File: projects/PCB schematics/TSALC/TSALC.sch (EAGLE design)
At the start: 27 parts, among them IC2 78L08SMD, IC4 NE555D, Q1 IRLZ44Z, Q2 IRLZ44Z, Q3 IRLZ44Z

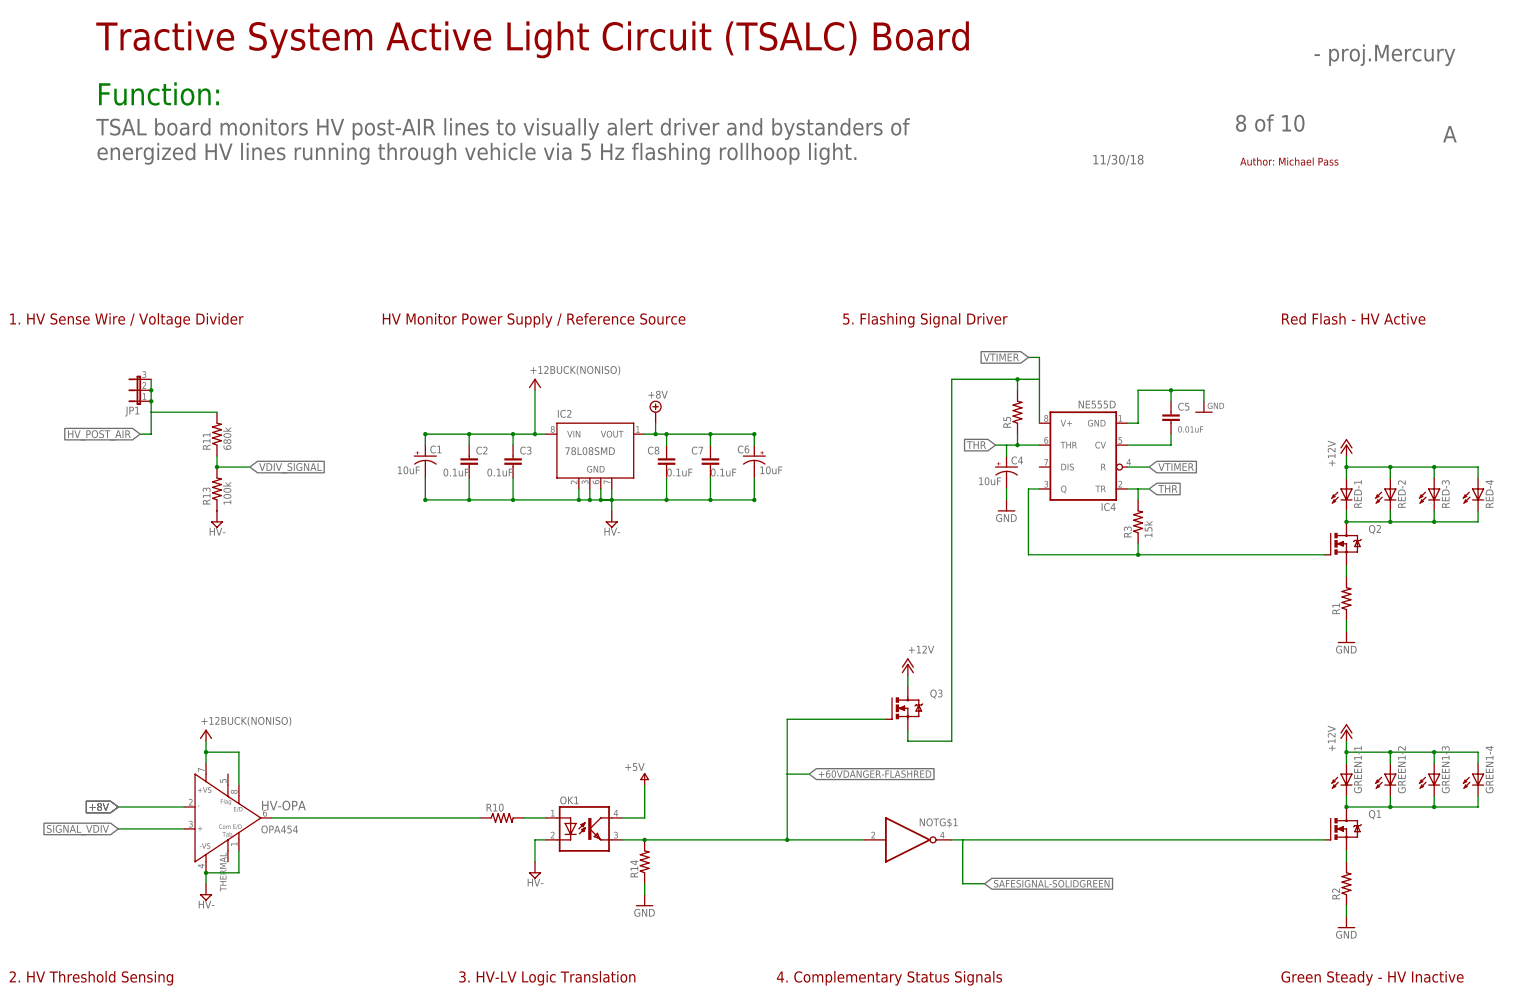
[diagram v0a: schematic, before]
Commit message: SC - Rev A; First PCB revision complete.
This marks the first draft of the SC board.
Parts have been laid out and initial routing completed through
extensive use of autorouter.
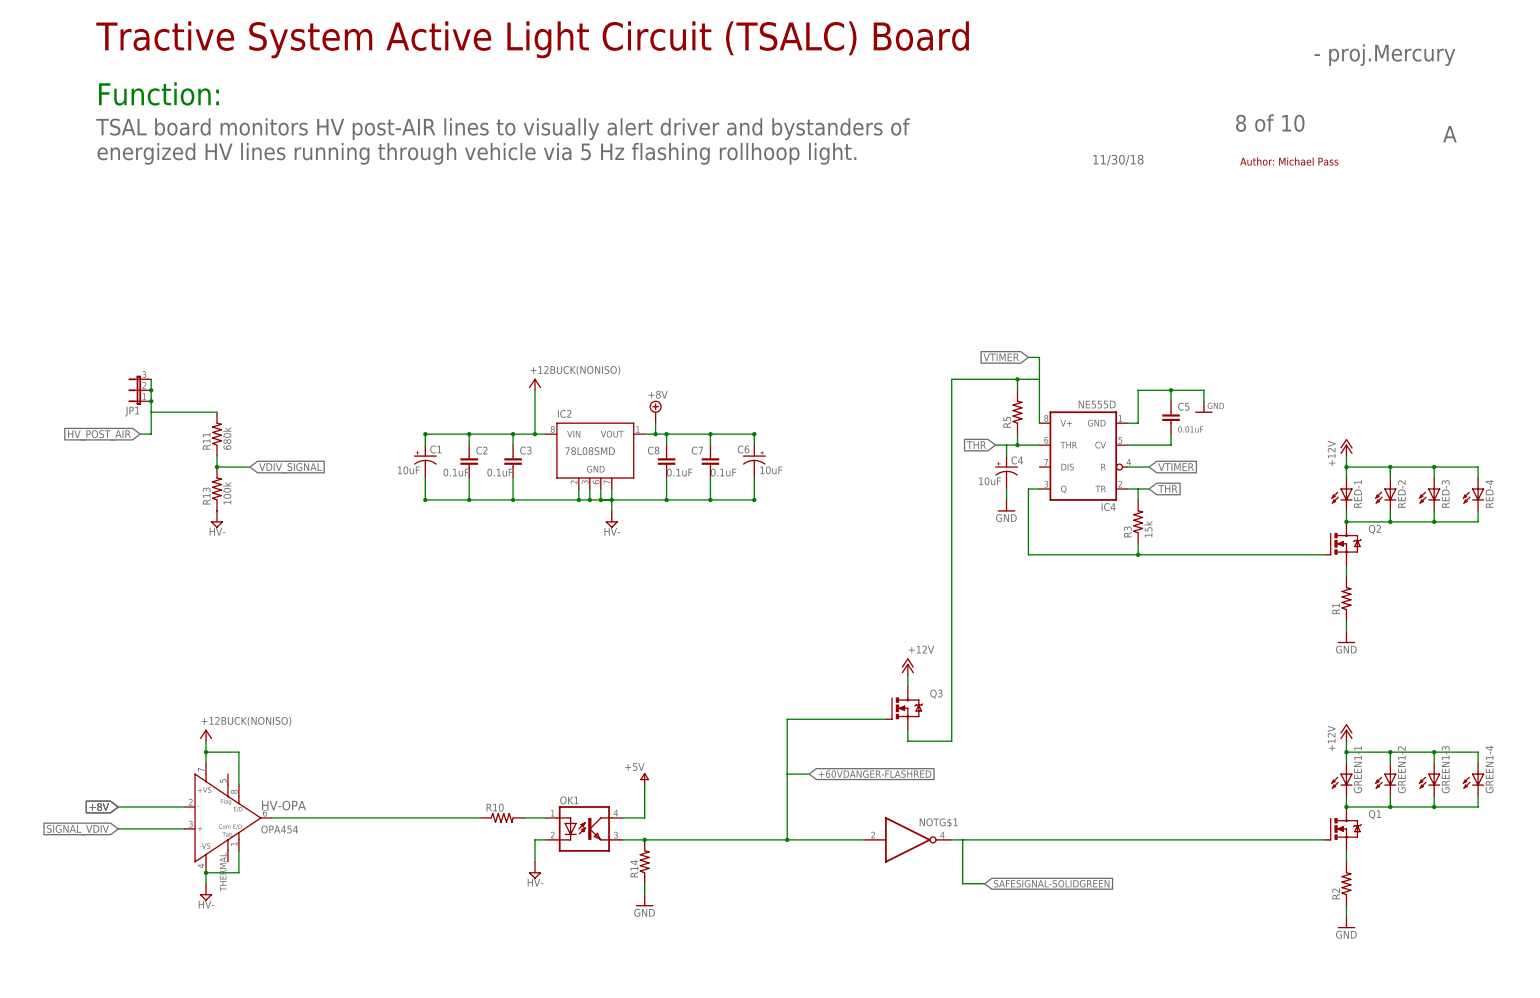
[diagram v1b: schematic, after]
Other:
- note removed: "1. HV Sense Wire / Voltage Divider"
- note removed: "2. HV Threshold Sensing"
- note removed: "3. HV-LV Logic Translation"
- note removed: "4. Complementary Status Signals"
- note removed: "5. Flashing Signal Driver"
- note removed: "Green Steady - HV Inactive"
- note removed: "HV Monitor Power Supply / Reference Source"
- note removed: "Red Flash - HV Active"
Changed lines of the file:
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@@
 <?xml version="1.0" encoding="utf-8"?>
 <!DOCTYPE eagle SYSTEM "eagle.dtd">
-<eagle version="9.3.0">
+<eagle version="9.3.1">
 <drawing>
 <settings>
@@
 <sheet>
 <plain>
-<frame x1="7.62" y1="7.62" x2="109.22" y2="81.28" columns="8" rows="5" layer="94" border-left="no" border-top="no" border-right="no" border-bottom="no"/>
-<text x="10.16" y="10.16" size="2.54" layer="94">2. HV Threshold Sensing</text>
-<frame x1="7.62" y1="7.62" x2="71.12" y2="15.24" columns="8" rows="5" layer="94" border-left="no" border-top="no" border-right="no" border-bottom="no"/>
-<frame x1="111.76" y1="7.62" x2="177.8" y2="81.28" columns="8" rows="5" layer="94" border-left="no" border-top="no" border-right="no" border-bottom="no"/>
-<text x="114.3" y="10.16" size="2.54" layer="94">3. HV-LV Logic Translation</text>
-<frame x1="111.76" y1="7.62" x2="177.8" y2="15.24" columns="8" rows="5" layer="94" border-left="no" border-top="no" border-right="no" border-bottom="no"/>
-<frame x1="7.62" y1="93.98" x2="91.44" y2="167.64" columns="8" rows="5" layer="94" border-left="no" border-top="no" border-right="no" border-bottom="no"/>
-<frame x1="93.98" y1="104.14" x2="198.12" y2="167.64" columns="8" rows="5" layer="94" border-left="no" border-top="no" border-right="no" border-bottom="no"/>
-<frame x1="200.66" y1="104.14" x2="294.64" y2="167.64" columns="8" rows="5" layer="94" border-left="no" border-top="no" border-right="no" border-bottom="no"/>
-<frame x1="302.26" y1="83.82" x2="360.68" y2="167.64" columns="8" rows="5" layer="94" border-left="no" border-top="no" border-right="no" border-bottom="no"/>
-<frame x1="302.26" y1="7.62" x2="360.68" y2="81.28" columns="8" rows="5" layer="94" border-left="no" border-top="no" border-right="no" border-bottom="no"/>
-<frame x1="185.42" y1="7.62" x2="294.64" y2="93.98" columns="8" rows="5" layer="94" border-left="no" border-top="no" border-right="no" border-bottom="no"/>
-<frame x1="0" y1="0" x2="368.3" y2="251.46" columns="8" rows="5" layer="91"/>
-<frame x1="7.62" y1="160.02" x2="71.12" y2="167.64" columns="8" rows="5" layer="94" border-left="no" border-top="no" border-right="no" border-bottom="no"/>
-<frame x1="93.98" y1="160.02" x2="175.26" y2="167.64" columns="8" rows="5" layer="94" border-left="no" border-top="no" border-right="no" border-bottom="no"/>
-<frame x1="185.42" y1="7.62" x2="241.3" y2="15.24" columns="8" rows="5" layer="94" border-left="no" border-top="no" border-right="no" border-bottom="no"/>
-<frame x1="302.26" y1="7.62" x2="360.68" y2="15.24" columns="8" rows="5" layer="94" border-left="no" border-top="no" border-right="no" border-bottom="no"/>
-<frame x1="302.26" y1="160.02" x2="360.68" y2="167.64" columns="8" rows="5" layer="94" border-left="no" border-top="no" border-right="no" border-bottom="no"/>
-<frame x1="200.66" y1="160.02" x2="271.78" y2="167.64" columns="8" rows="5" layer="94" border-left="no" border-top="no" border-right="no" border-bottom="no"/>
-<text x="10.16" y="162.56" size="2.54" layer="94">1. HV Sense Wire / Voltage Divider</text>
-<text x="187.96" y="10.16" size="2.54" layer="94">4. Complementary Status Signals</text>
-<text x="96.52" y="162.56" size="2.54" layer="94">HV Monitor Power Supply / Reference Source</text>
-<text x="203.2" y="162.56" size="2.54" layer="94">5. Flashing Signal Driver</text>
-<text x="304.8" y="162.56" size="2.54" layer="94">Red Flash - HV Active</text>
-<text x="304.8" y="10.16" size="2.54" layer="94">Green Steady - HV Inactive</text>
 <text x="30.48" y="226.06" size="6.4516" layer="94">Tractive System Active Light Circuit (TSALC) Board</text>
 <text x="30.48" y="213.36" size="5.08" layer="91">Function:</text>

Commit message: TSALC - Initial build.
Initial build done by Anshuman. 
TSALC is still WIP.
TSALC work must be continued on another branch.
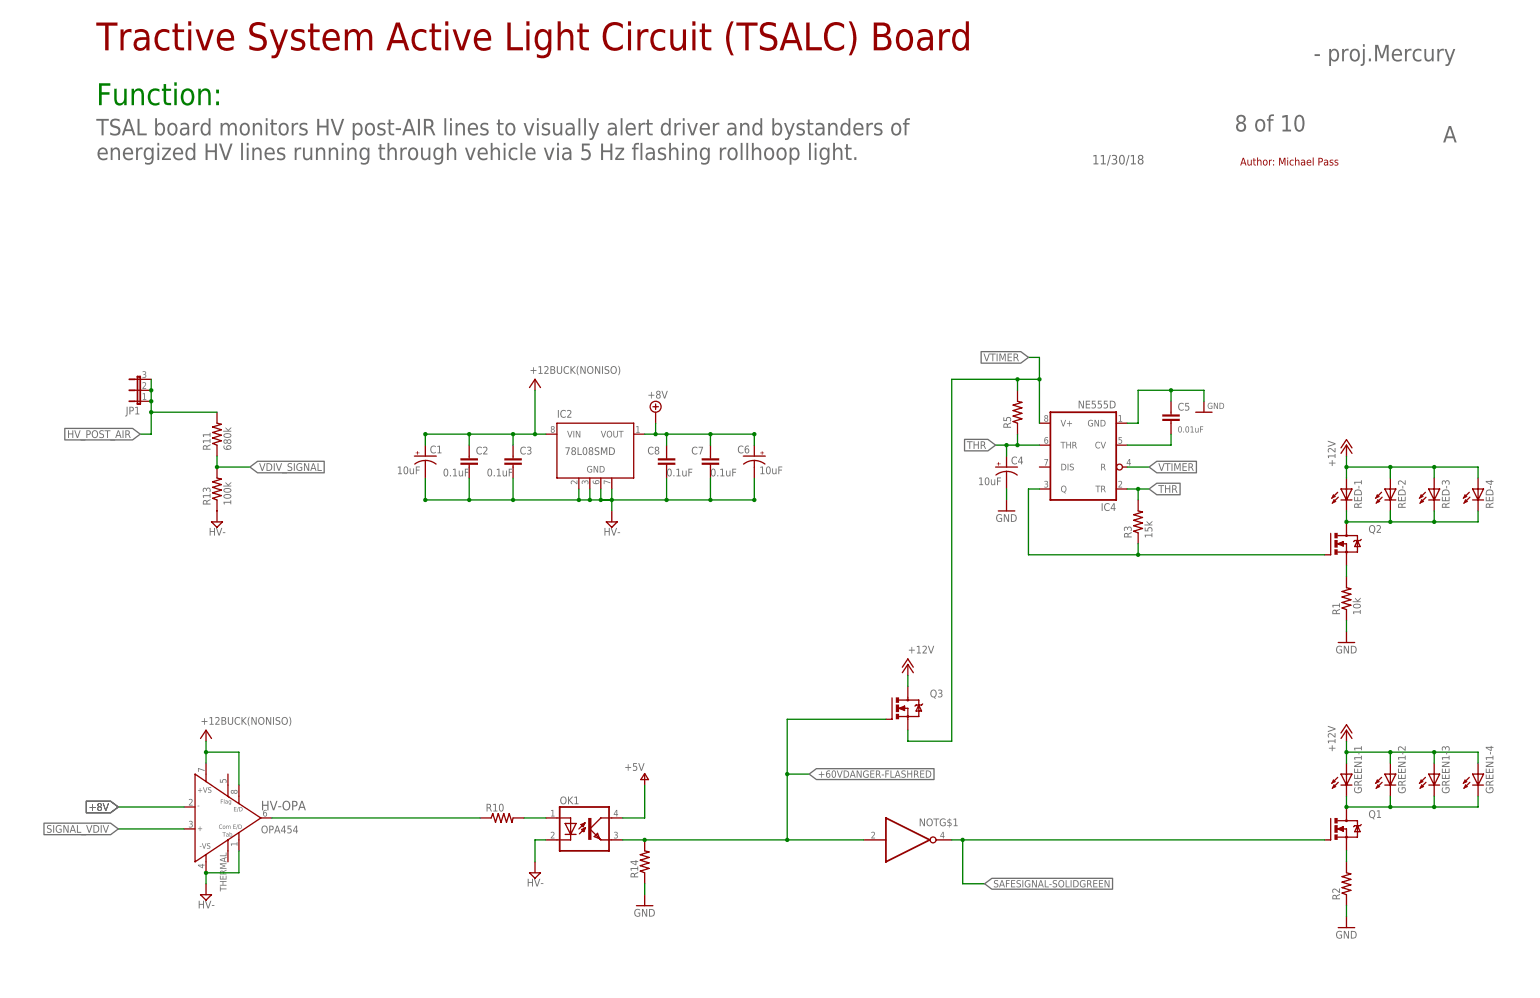
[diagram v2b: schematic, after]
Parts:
- R1: value (none) -> 10k
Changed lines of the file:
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@@
 <?xml version="1.0" encoding="utf-8"?>
 <!DOCTYPE eagle SYSTEM "eagle.dtd">
-<eagle version="9.3.1">
+<eagle version="9.3.2">
 <drawing>
 <settings>
@@
 <setting verticaltext="up"/>
 </settings>
-<grid distance="0.1" unitdist="inch" unit="inch" style="lines" multiple="1" display="no" altdistance="0.01" altunitdist="inch" altunit="inch"/>
+<grid distance="0.1" unitdist="inch" unit="inch" style="lines" multiple="1" display="yes" altdistance="0.01" altunitdist="inch" altunit="inch"/>
 <layers>
 <layer number="1" name="Top" color="4" fill="1" visible="no" active="no"/>
@@
 <part name="C4" library="rcl" library_urn="urn:adsk.eagle:library:334" deviceset="CPOL-US" device="085CS-1AW" package3d_urn="urn:adsk.eagle:package:23385/1" value="10uF"/>
 <part name="C5" library="rcl" library_urn="urn:adsk.eagle:library:334" deviceset="C-EU" device="C0805" package3d_urn="urn:adsk.eagle:package:23617/2" value="0.01uF"/>
-<part name="R1" library="rcl" library_urn="urn:adsk.eagle:library:334" deviceset="R-US_" device="R0805" package3d_urn="urn:adsk.eagle:package:23553/2"/>
+<part name="R1" library="rcl" library_urn="urn:adsk.eagle:library:334" deviceset="R-US_" device="R0805" package3d_urn="urn:adsk.eagle:package:23553/2" value="10k"/>
 <part name="Q1" library="transistor-power" library_urn="urn:adsk.eagle:library:400" deviceset="IRLZ44Z" device="" package3d_urn="urn:adsk.eagle:package:29490/1"/>
 <part name="GND2" library="supply1" library_urn="urn:adsk.eagle:library:371" deviceset="GND" device=""/>
@@
 <wire x1="43.18" y1="137.16" x2="40.64" y2="137.16" width="0.1524" layer="91"/>
 <label x="40.64" y="137.16" size="1.778" layer="95" rot="R180" xref="yes"/>
+<junction x="43.18" y="142.24"/>
 </segment>
 </net>
@@
 <label x="195.58" y="58.42" size="1.6764" layer="95" xref="yes"/>
 <wire x1="190.5" y1="58.42" x2="195.58" y2="58.42" width="0.1524" layer="91"/>
+<junction x="190.5" y="58.42"/>
 </segment>
 </net>
@@
 <wire x1="243.84" y1="149.86" x2="243.84" y2="147.32" width="0.1524" layer="91"/>
 <junction x="243.84" y="149.86"/>
+<junction x="248.92" y="149.86"/>
 </segment>
 <segment>
@@
 <wire x1="271.78" y1="124.46" x2="274.32" y2="124.46" width="0.1524" layer="91"/>
 <label x="274.32" y="124.46" size="1.778" layer="95" xref="yes"/>
+<junction x="271.78" y="124.46"/>
 </segment>
 <segment>
@@
 <wire x1="243.84" y1="137.16" x2="243.84" y2="134.62" width="0.1524" layer="91"/>
 <junction x="243.84" y="134.62"/>
+<junction x="241.3" y="134.62"/>
 </segment>
 </net>
@@
 <wire x1="231.14" y1="43.18" x2="231.14" y2="33.02" width="0.1524" layer="91"/>
 <wire x1="231.14" y1="33.02" x2="236.22" y2="33.02" width="0.1524" layer="91"/>
+<junction x="231.14" y="43.18"/>
 </segment>
 </net>
@@
 </sheet>
 </sheets>
+<errors>
+</errors>
 </schematic>
 </drawing>

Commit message: Minor board update
Cleared up come wiring conflicts
Board Schematic Update

555 Timer Circuit changed accordingly.
(ref. https://www.allaboutcircuits.com/tools/555-timer-astable-circuit/)
Flash Frequency = 4.80 Hz
Duty Cycle = 66.67%
Board Revision Update( Rev B)

Both board and schematic updated.
Clearance issues still remain.
Some component values need to be verified again.
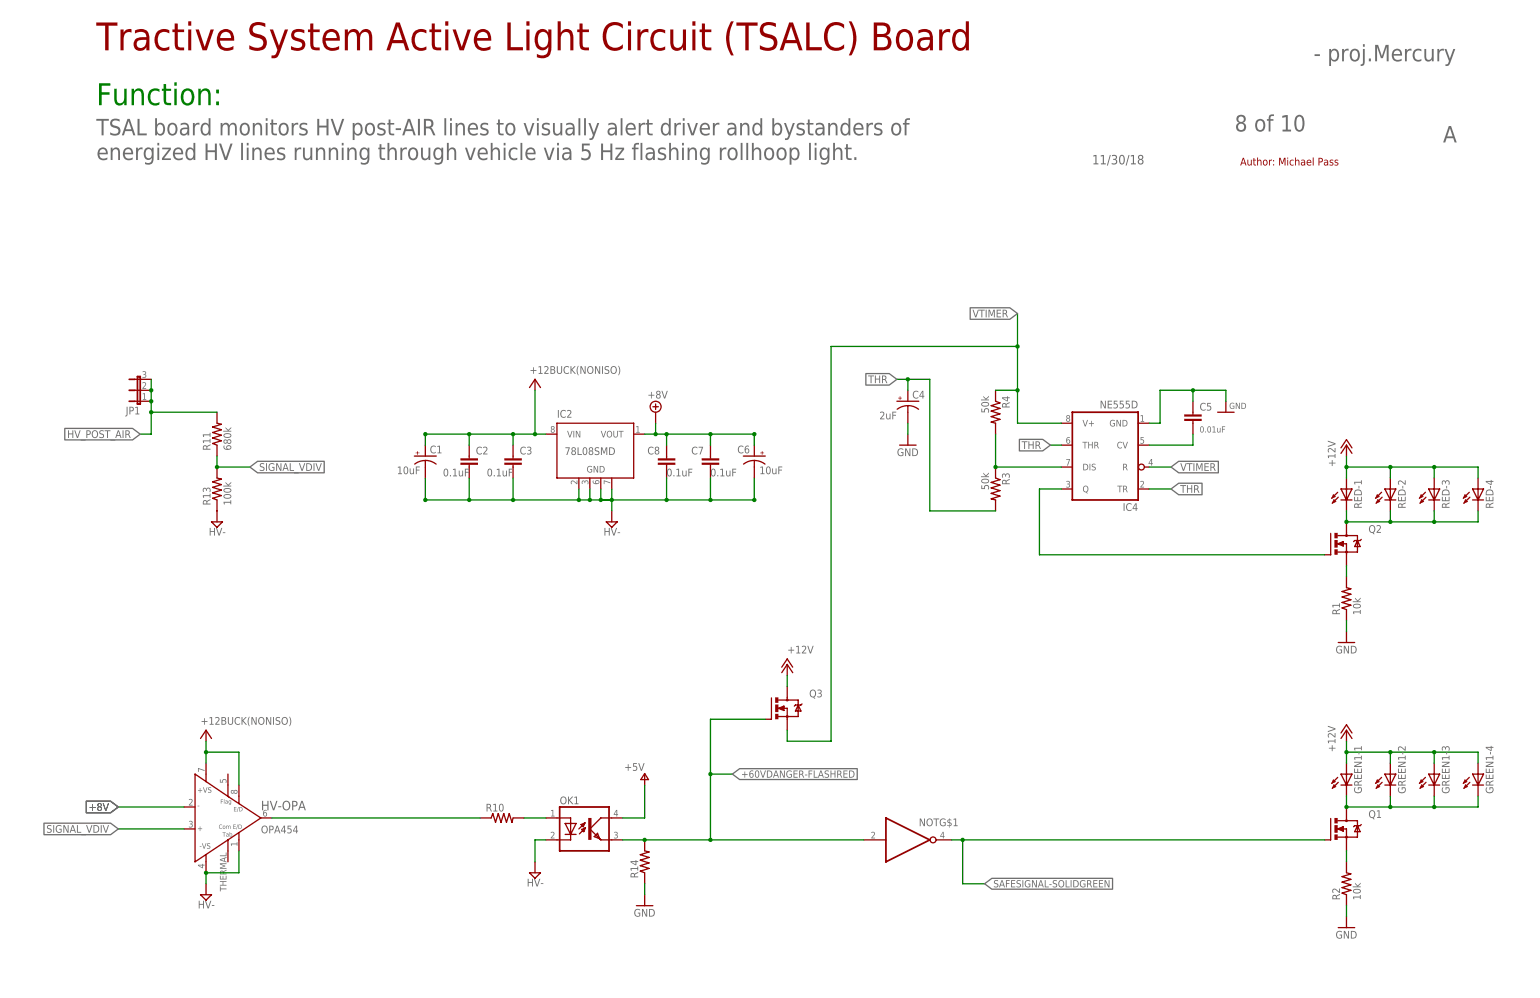
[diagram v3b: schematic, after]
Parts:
- removed R5: (no value), rcl:R-US_R0805
- added R4: 50k, rcl:R-US_R0805
- C4: value 10uF -> 2uF
- R2: value (none) -> 10k
- R3: value 15k -> 50k
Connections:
- removed net VDIV_SIGNAL: R11.1, R13.2
- new net N$2: IC4.DIS, R3.1, R4.2
- net N$8: no longer R3.1
- net SIGNAL_VDIV: now also R11.1, R13.2
- net THR: no longer R5.1
- net VTIMER: now also R4.1; no longer R5.2
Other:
- moved on the sheet: C4, C5, IC4, Q3, R3
